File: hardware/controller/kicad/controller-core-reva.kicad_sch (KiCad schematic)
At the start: 187 parts, among them J101 12V_ISOLATED_INPUT / JST XH, J102 STM_SWD / 1x6 2.54mm, J103 ESP_UART / 1x6 2.54mm, J104 UI_LINK / IDC 2x8 2.54mm, J105 JP13 NTC / 2 vías, J106 JP5 FLOW ADAPTER / VCC-GND-OC, J107 JP14 DOOR / contacto seco, J108 JP16 VISUAL V1..V8 / XH-8, J109 JP22 WATER / RED-WHITE-BLACK, J110 USB-C SERVICE / USB 2.0, J111 USB BENCH POWER / OPEN, J112 24V_ACTUATOR_INPUT / JST XH, J113 JP3 VALVE / A2506, J114 POWER MONITOR / MEASURE ONLY, J115 JP8 GRINDER / 320VDC, J116 JP19 HEATER / 1900W 27R5, J117 JP24 PUMP / 230VAC, J118 JP17 MAINS / L-N, J119 JP1 PE TO BOILER, J120 JP9 PE INPUT, J121 24V INTERNAL SELECT / OPEN FO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, K701 G5RL-1A-E-TV8 DC24, Q501 SI2308A, Q701 SI2308A / relay coil, Q703 BTA24-800BWRG / heater, Q704 BTA24-800BWRG / pump, Q705 SI2308A / heater opto LED, Q706 SI2308A / pump opto LED, Q707 SI2308A / grinder opto LED, Q708 BTA24-800BWRG / grinder, U101 STM32G431RBT6, U201 ESP32-S3-WROOM-1U-N8R8, U203 USBLC6-2SC6, U301 AP63203WU-7, U302 TPS22918DBVR, U303 AP63200WU-7 / 24V to 12V, U501 DRV8876PWPR, U502 UCC27517DBVR, U601 TPS3828-33DBVR, U602 SN74LVC2G08DCTR, U603 SN74LVC2G08DCTR, U604 SN74LVC2G08DCTR, U701 MOC3083 / zero-cross, U702 MOC3083 / zero-cross, U703 MOC3083 / zero-cross

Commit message: Bring the documentation in line with the routed board
A full reread against the schematic, BOM, PCB and validation reports.

Data errors: the flowmeter is on PA2 (TIM2_CH3) and the water level on
PC3, not PA1/PA2; the ESP32 UART is on IO42/IO2 and VBUS sensing on IO15,
not IO17/IO18/IO21; the brew current is read on PC0, not PA3; the ESP32
code in the assembly notes is C2980300; the discarded VOT8125 row goes;
the 27.5 ohm heater reading joins the measurement log.

Stale state: footprint counts of 135 to 159, unrouted connections, a
"partial schematic", undrawn mains stages and pending fills and
silkscreen give way to the current 187-position routed board. The
controller README, core-design and kicad-workflow are largely rewritten;
io-map and connectors.csv now carry each connector's MCU pin, and the
watchdog note lists all four U603/U604 gates.

The schematic's own notes are updated in the generator and the schematic
regenerated (ERC 0, netlist 187/612). validate_kicad.py no longer calls
the schematics partial and reads its routing counts from routing.json.

Open design point, recorded but unchanged: J101 shares its node with the
U303 output with no diode or selector.

Co-Authored-By: Claude Opus 5.5 <noreply@anthropic.com>
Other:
- note added: "BORRADOR: lógica, USB, sensores, cargas de 24V y de red y fuente IRM-30 en la misma placa. Sin ensayar."
- note added: "Contorno/taladros aceptados; PCB ruteada con DRC limpio, sin ensayar. JP14/JP16/JP22 sin identificar. BOM no liberada."
- note added: "J101 solo desde una fuente AC/DC aislada y certificada; en la máquina los 12V salen de U303 (hoja 15)."
- note added: "NC = pin sin asignar; no equivale a ninguna vía del arnés Saeco."
- note added: "OPEN SAECO / PRINCIPAL — REV A"
- note added: "Siguiente: filtro EMI, valores de F701/F702/RV701 y medidas de caracterización del molino."
- note removed: "BORRADOR PARCIAL: lógica, USB, sensores y dos cargas de 24V. La principal final integra red."
- note removed: "Contorno/taladros aceptados; conectores incompletos y rutas pendientes. BOM no liberada."
- note removed: "Entrada exclusivamente desde una fuente AC/DC aislada y certificada; el módulo de red aún no está seleccionado."
- note removed: "NC = sin asignar en esta hoja parcial; revisar al integrar sensores y drivers."
- note removed: "OPEN SAECO / PRINCIPAL — NÚCLEO LÓGICO A.0"
- note removed: "Siguiente: filtro EMI, huellas PE y medidas de caracterización del molino."

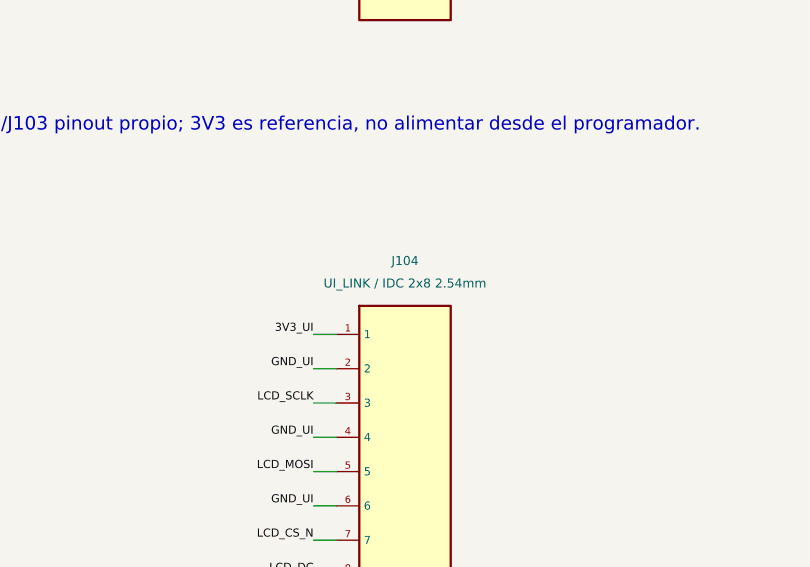
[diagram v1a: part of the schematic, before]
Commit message: Fit the owner-identified Wurth WR-MM front-panel link on both boards
The owner identified the connector of the original link between the main
board and the front panel as Wurth WR-MM 690367181672 (16 contacts at
1.27 mm stagger), the same part at both ends of a 1:1 16-wire flat cable.
The latch of the cable plug enters a 1.5 mm hole beside pin 1, which locks
it and sets its direction, so pin 1 always meets pin 1. It replaces the
2x8 IDC in J104 and J1. JLCPCB lists it as C19103863, without stock.

The footprint follows Wurth drawing 690367181672 rev 002.000: 0.85 mm
holes, 1.4 mm pads, a 22.32 x 5 mm body and the 1.5 mm non-plated latch
hole; it gets a 6.1 mm tall stand-in model shared by both boards.

- Main board: J104 turns 180 deg with pin 1 on the IDC's pin 1, so the
  odd pins stay and the even pins move 1.27 mm east. 3V3_UI passes west of
  the latch hole; DC, BL and SDA reach their new pins and SCL and INT end on
  the pad centres. 1315 segments, 439 vias.
- Front panel: J1 is centred on the original JP3 zone, C3 stays by pin 1,
  rerouted by Freerouting (297 segments, 192 vias); fab package refreshed.

The photo count of 20 contacts for JP21 was wrong. ERC 0 on both boards;
netlists 187/612 and 42/118. DRC with all severities: main 0 violations,
0 unconnected, parity only MH1-MH3; front 0/0/0. Still to do: try the
cable latch in both new boards; 3V3_UI rides one 1.5 A contact.

Co-Authored-By: Claude Opus 5.5 <noreply@anthropic.com>
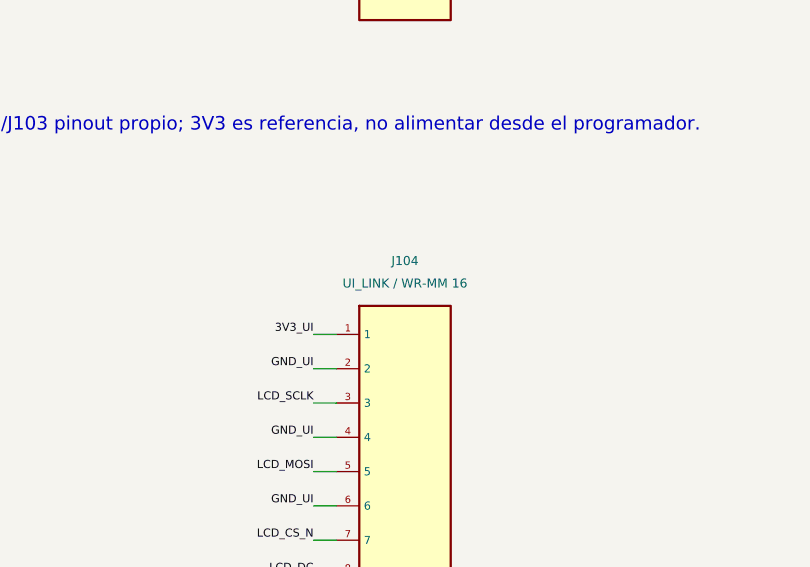
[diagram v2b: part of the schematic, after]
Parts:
- J104: value UI_LINK / IDC 2x8 2.54mm -> UI_LINK / WR-MM 16; footprint Connector_IDC:IDC-Header_2x08_P2.54mm_Vertical -> OpenSaeco:Wurth_WR-MM_690367181672_2x08_P1.27mm_Vertical; lcsc C7501244 -> C19103863; manufacturer Megastar -> Wurth Elektronik; mpn ZX-IDC2.54-2-8PZZ -> 690367181672; pcba_type Economic and Standard -> TBD

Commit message: Take the JLC library class of every catalogued part from JLCPCB
refresh_jlc_stock.py reported eleven parts whose catalog class did not
match JLCPCB's library type on 2026-10-01. The catalog now follows JLCPCB:

- Basic to Extended: R 2.49k (C22908) and R 16k (C4210).
- TBD to Extended: DRV8876PWPR, UCC27517DBVR, SI2308A, TPS3828-33DBVR,
  SN74LVC2G08DCTR, 1206L050YR, AP63200WU-7 and SRP7028A-100M.
- TBD to Basic: R 18k (C25810).

The class reaches the main-board schematic, BOM, netlist and footprint
fields; the front panel uses none of these parts. The assembly README now
gives the library class for every row whose PCBA type is still to verify.
ERC 0, netlist 187/612; DRC with all severities unchanged: 0 violations,
0 unconnected, parity only MH1-MH3.

Co-Authored-By: Claude Opus 5.5 <noreply@anthropic.com>
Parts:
- F302, L302, Q501, Q701, Q705, Q706, Q707, U303, U501, U502, U601, U602, U603, U604: jlc_class TBD -> Extended
- R303: jlc_class TBD -> Basic
- R508, R510: jlc_class Basic -> Extended

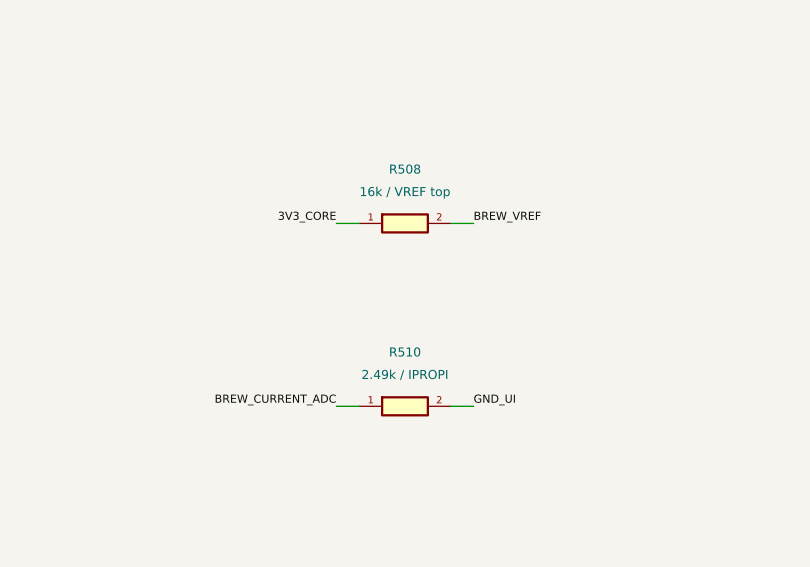
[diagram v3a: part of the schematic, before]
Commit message: Move the DRV8876 current-limit resistors to JLCPCB Basic values
R510 (IPROPI) goes from 2.49k (C22908) to 2.4k (C22940) and R508 (VREF
high side) from 16k (C4210) to 18k (C25810, the part R303 already uses).
Both old values became Extended at JLCPCB; the new ones are Basic, so the
main board loses two Extended lines.

With R509 = 49.9k, VREF = 3.3 x 49.9 / 67.9 = 2.425 V (was 2.498 V) and,
at 1000 uA/A, I_TRIP = 2.425 / 2.4 = 1.01 A (was 1.00 A). IPROPI reads
about 1.2 V at 0.5 A; firmware converts with I = V / 2.4.

Same 0603 footprint, so placement and routing are untouched; the PCB only
takes the new value and sourcing fields. The stock script refreshed the
catalog again on the way. ERC 0, netlist 187/612; DRC with all severities:
0 violations, 0 unconnected, parity only MH1-MH3.

Co-Authored-By: Claude Opus 5.5 <noreply@anthropic.com>
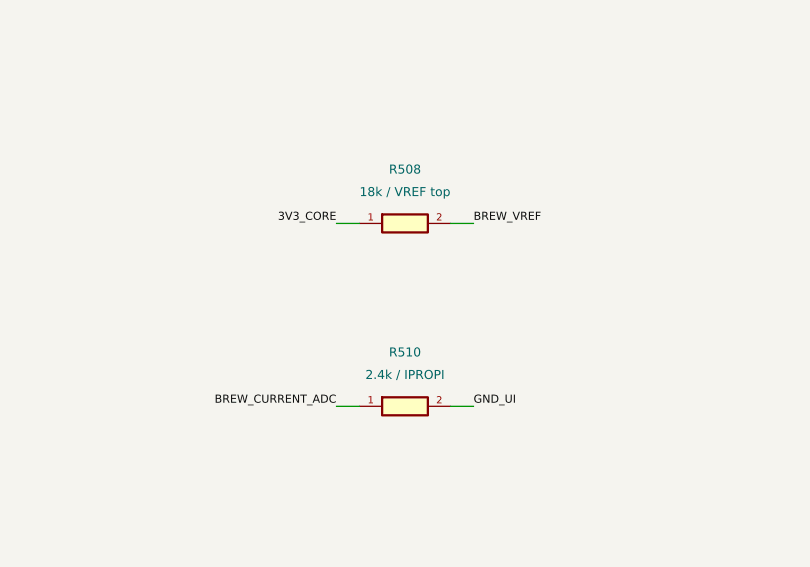
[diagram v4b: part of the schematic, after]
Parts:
- R508: value 16k / VREF top -> 18k / VREF top; jlc_class Extended -> Basic; lcsc C4210 -> C25810; mpn 0603WAF1602T5E -> 0603WAF1802T5E; pcba_type Economic and Standard -> TBD
- R510: value 2.49k / IPROPI -> 2.4k / IPROPI; jlc_class Extended -> Basic; lcsc C22908 -> C22940; mpn 0603WAF2491T5E -> 0603WAF2401T5E

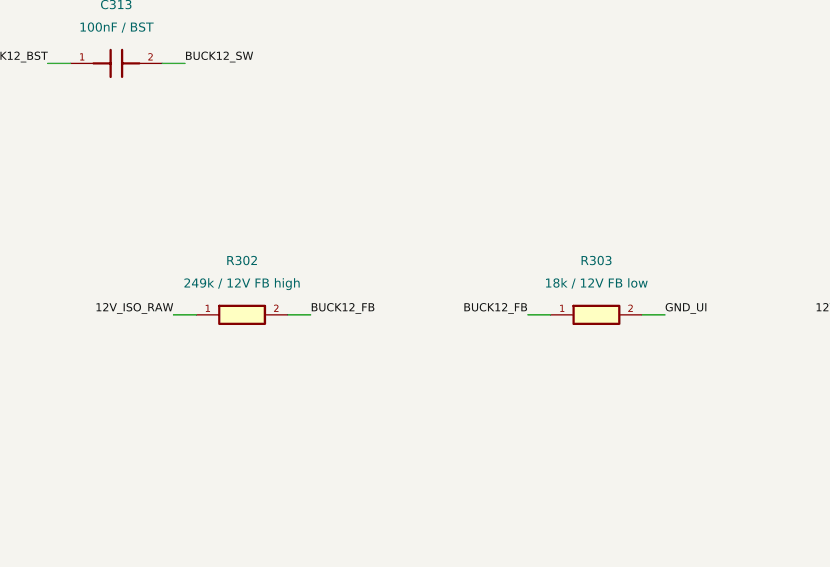
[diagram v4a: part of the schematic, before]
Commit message: Move the 12 V buck feedback divider to JLCPCB Basic values
A sweep of every catalogued resistor left two Extended parts. R302/R303,
the AP63200 feedback divider, go from 249k (C22918, Extended)/18k to
330k (C23137)/24k (C23352), both Basic. Eq. 6 of the Diodes datasheet
gives VOUT = 0.8 x (1 + 330/24) = 11.80 V, against 11.87 V for the
table's 249k/18k; C314 stays 56 pF, inside the 10-220 pF the datasheet
allows for the feed-forward capacitor.

R710, R712 and R721, the triac gate resistors on the mains side, stay
Panasonic ERJ-P08J391V: they need 500 V limiting voltage and 0.83 A
pulses, and the Basic 1206 parts are plain thick film of about 200 V.

Same 0603 footprint, so placement and routing are untouched. The stock
script refreshed the catalog on the way. ERC 0, netlist 187/612; DRC with
all severities: 0 violations, 0 unconnected, parity only MH1-MH3.

Co-Authored-By: Claude Opus 5.5 <noreply@anthropic.com>
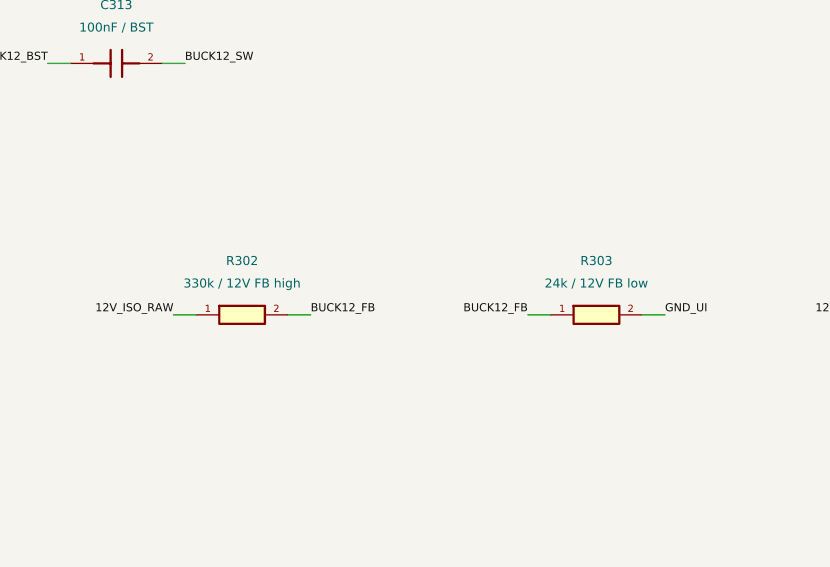
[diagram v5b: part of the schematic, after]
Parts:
- R302: value 249k / 12V FB high -> 330k / 12V FB high; jlc_class Extended -> Basic; lcsc C22918 -> C23137; mpn 0603WAF2493T5E -> 0603WAF3303T5E
- R303: value 18k / 12V FB low -> 24k / 12V FB low; lcsc C25810 -> C23352; mpn 0603WAF1802T5E -> 0603WAF2402T5E; pcba_type TBD -> Economic and Standard

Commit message: Add the board model for the firmware simulator and fix what it found
F0 of the simulator: tools/build_board_model.py joins both KiCad netlists
through the J104/J1 harness and checks them against a firmware contract
(firmware/common/signals.json) and vendor pinouts (sim/reference/). It
resolves every firmware signal to its physical pad, peripheral, AF and ADC
channel, traces each order to its load and through the watchdog AND gate,
solves the reset levels and the analog inputs by nodal analysis, and
checks the harness and the TCA9534 keypad. It generates board_pins.h for
both MCUs, sim/board-model.json for F1 and sim/board-report.md. Stdlib
only; 20 mutation tests in tests/sim and a C test of the header. CI runs
both.

Its first run found three errors on the main board:

- U101: pads 12-29 followed the F-series LQFP64. The G431 has PA0-PA2 on
  12-14, VSS/VDD on 15/16 and VSSA/VREF+/VDDA on 27-29 (ST
  STM32_open_pin_data, identical to KiCad's STM32G431R_6-8-B_Tx). As
  routed, VSS sat on DOOR_CLOSED_N, VDD on FLOW_TIM and VSSA/VREF+/VDDA
  were open. check_controller_core.py held the same wrong table.
- U502: the UCC27517 DBV is 1 VDD, 2 GND, 3 IN+, 4 IN-, 5 OUT (TI
  SLUSAY4D); the symbol put the output on the 12 V rail.
- MAINS_ARM_RAW (PB7 -> U603.1A) floated after reset. R722 = 10k (C25804,
  Basic) pulls it down like the other five orders.

The firmware assignment is kept except the heater order, which moves from
PB10 to PC5 so C107 (10 nF) can sit under VREF+/VDDA. The MCU corner, the
bottom row, U502 and R722 are re-routed in route_controller_pcb.py. C102
now decouples VDD16 through the planes from across the PA0-PA2 escapes;
worth a look in the 1:1 check. sync_controller_pcb.py finds the stock
footprints on Windows too.

ERC 0 on both boards; netlist 188/614; DRC with all severities: 0
violations, 0 unconnected, parity only MH1-MH3; board model 0 errors,
0 warnings.

Co-Authored-By: Claude Opus 5.5 <noreply@anthropic.com>
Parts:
- added R722: 10k / mains arm pull-down, Resistor_SMD:R_0603_1608Metric, symbol OpenSaeco:R
- C102: value 100nF / VDD13 -> 100nF / VDD16
- C107: value 10nF / VDDA20 -> 10nF / VDDA29
- C108: value 1uF / VDDA20 -> 1uF / VDDA29
- C109: value 100nF / VREF19 -> 100nF / VREF28
- C110: value 1uF / VREF19 -> 1uF / VREF28
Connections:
- net 12V_PROTECTED: now also U502.1 (VDD); no longer U502.5 (VDD)
- net 3V3_CORE: now also U101.16 (VDD), U101.28 (VREF+), U101.29 (VDDA); no longer U101.13 (VDD), U101.19 (VREF+), U101.20 (VDDA)
- net BU_WORK_N: now also U101.12 (PA0); no longer U101.14 (PA0)
- net DOOR_CLOSED_N: now also U101.13 (PA1); no longer U101.15 (PA1)
- net FLOW_TIM: now also U101.14 (PA2); no longer U101.16 (PA2)
- net GND_UI: now also U101.15 (VSS), U101.27 (VSSA), U502.4 (IN-), R722.2; no longer U101.12 (VSS), U101.18 (VSSA), U502.3 (IN-)
- net GRINDER_EN_RAW: now also U101.22 (PC4); no longer U101.25 (PC4)
- net HEATER_EN_RAW: now also U101.23 (PC5); no longer U101.30 (PB10)
- net MAINS_ARM_RAW: now also R722.1
- net VALVE_EN_DRV: now also U502.3 (IN+); no longer U502.1 (IN+)
- net VALVE_EN_RAW: now also U101.21 (PA7); no longer U101.24 (PA7)
- net VALVE_GATE_RAW: now also U502.5 (OUT); no longer U502.4 (OUT)
